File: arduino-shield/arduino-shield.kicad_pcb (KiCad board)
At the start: 2 copper layers, 92 x 61 mm, 15 parts, among them J1 393800102, J2 393800102, J3 393800102, Q1 TIP120, Q2 TIP120, SW1 100SP4T1B2M2QE, SW2 100SP4T1B2M2QE, SW3 ANT13SECQE

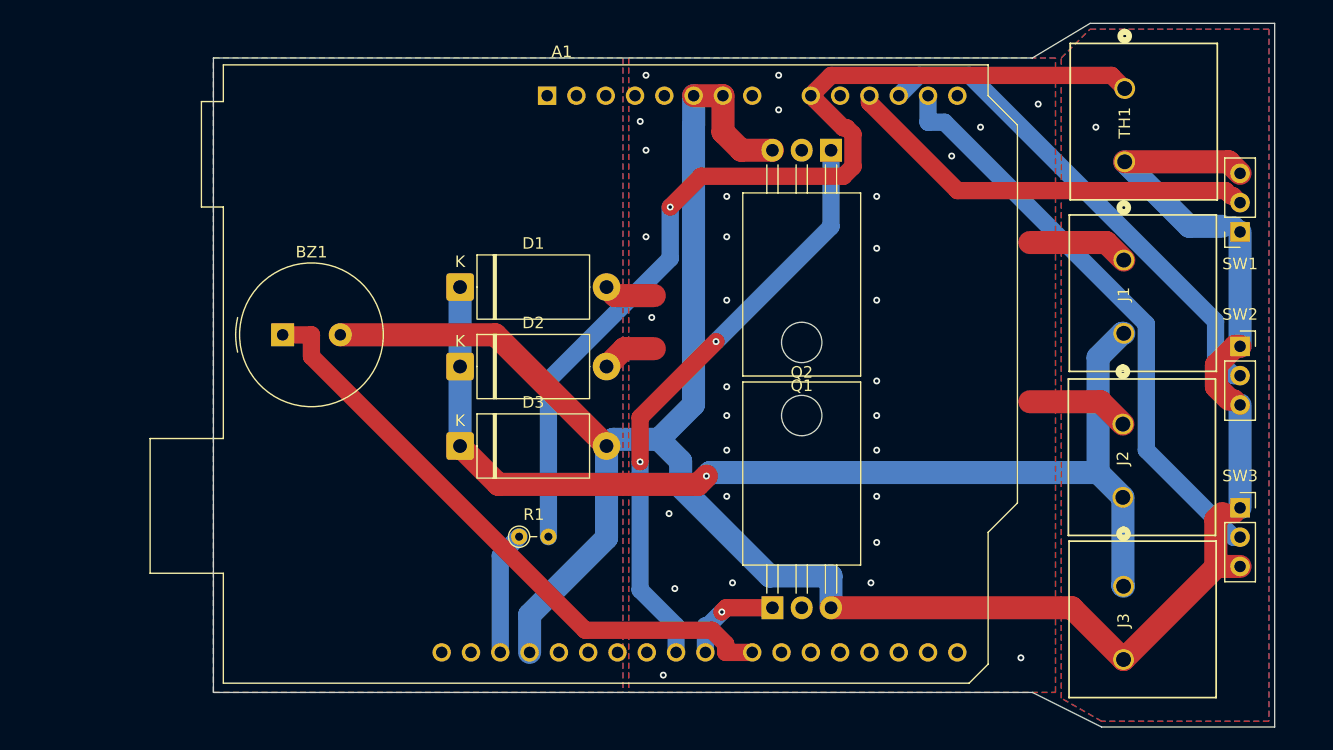
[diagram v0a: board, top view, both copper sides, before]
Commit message: Expand BOM and assembly docs; add shield placement image.
Document DigiKey line items, step-by-step assembly with arduino-shield.jpg,
nylon M3 mounting for Q1/Q2, and updated shield Gerbers/KiCad exports.

Co-authored-by: Cursor <cursoragent@cursor.com>
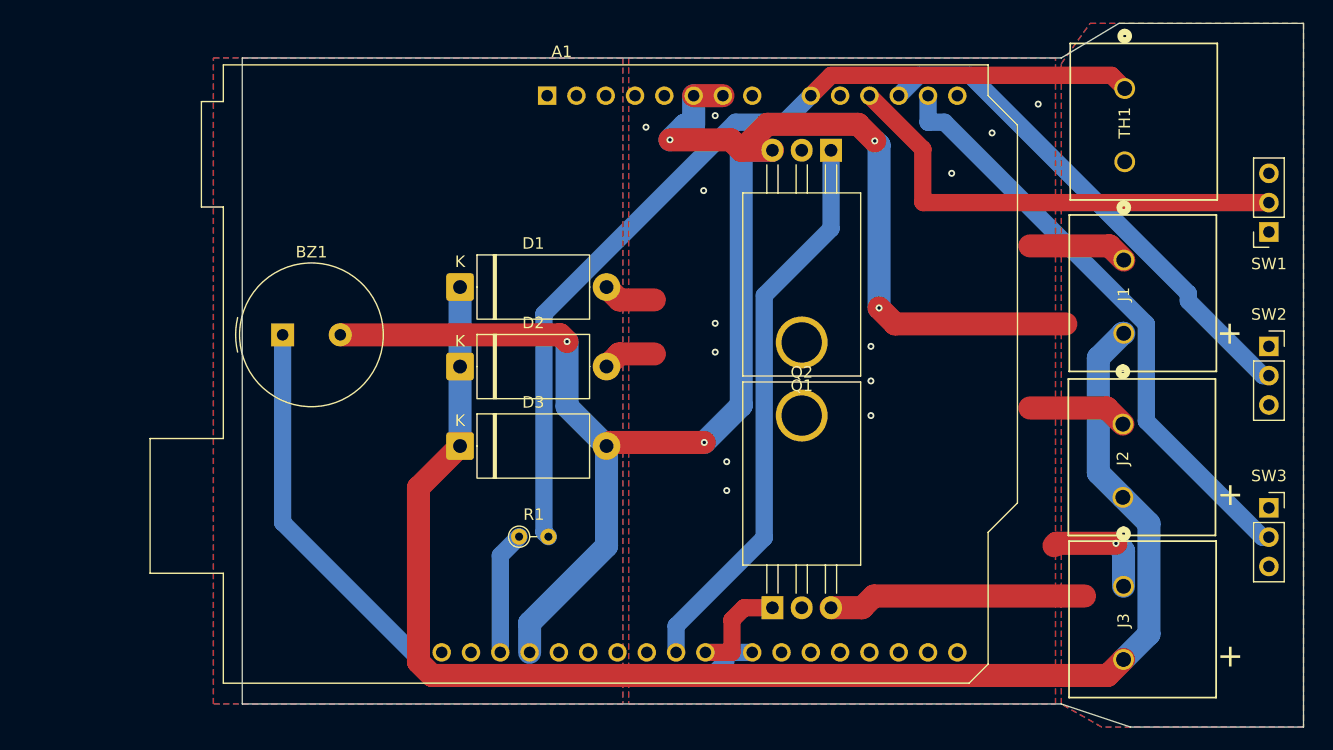
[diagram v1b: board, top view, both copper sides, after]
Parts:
- moved SW1 2.50 mm to (194.5, 82.1)
- moved SW2 2.50 mm to (194.5, 92.0)
- moved SW3 2.50 mm to (194.5, 106.0)
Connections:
- J3 pad 1: 12vdc -> /current
- J3 pad 2: GND -> 12vdc
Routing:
- net GND: track 214.4 -> 172.8 mm, vias 0 -> 5
- net 12vdc: track 94.7 -> 128.1 mm, vias 1 -> 0
- net buzzer+: track 53.6 -> 63.8 mm
- net /current: track 26.9 -> 36.0 mm, vias 31 -> 14
- net Vsense: track 86.5 -> 78.9 mm, vias 1 -> 0
- net temp_up: track 36.3 -> 41.2 mm
- net pump-pwm: track 51.7 -> 49.1 mm, vias 2 -> 0
- net temp_down: track 42.9 -> 44.0 mm
- net relay_control: track 50.6 -> 51.7 mm
- net relay2pin: track 8.76 -> 9.06 mm, vias 1 -> 0
- net (no net): vias 1 -> 0
- added copper zone on B.Cu, net GND
- added copper zone on F.Cu, net GND
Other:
- outline, holes or cut-outs redrawn
- board text added: "+"

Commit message: Update shield layout, placement image, and Gerbers.
Refresh KiCad PCB, silkscreen, and fabrication outputs to match the
current board design shown in arduino-shield.jpg.

Co-authored-by: Cursor <cursoragent@cursor.com>
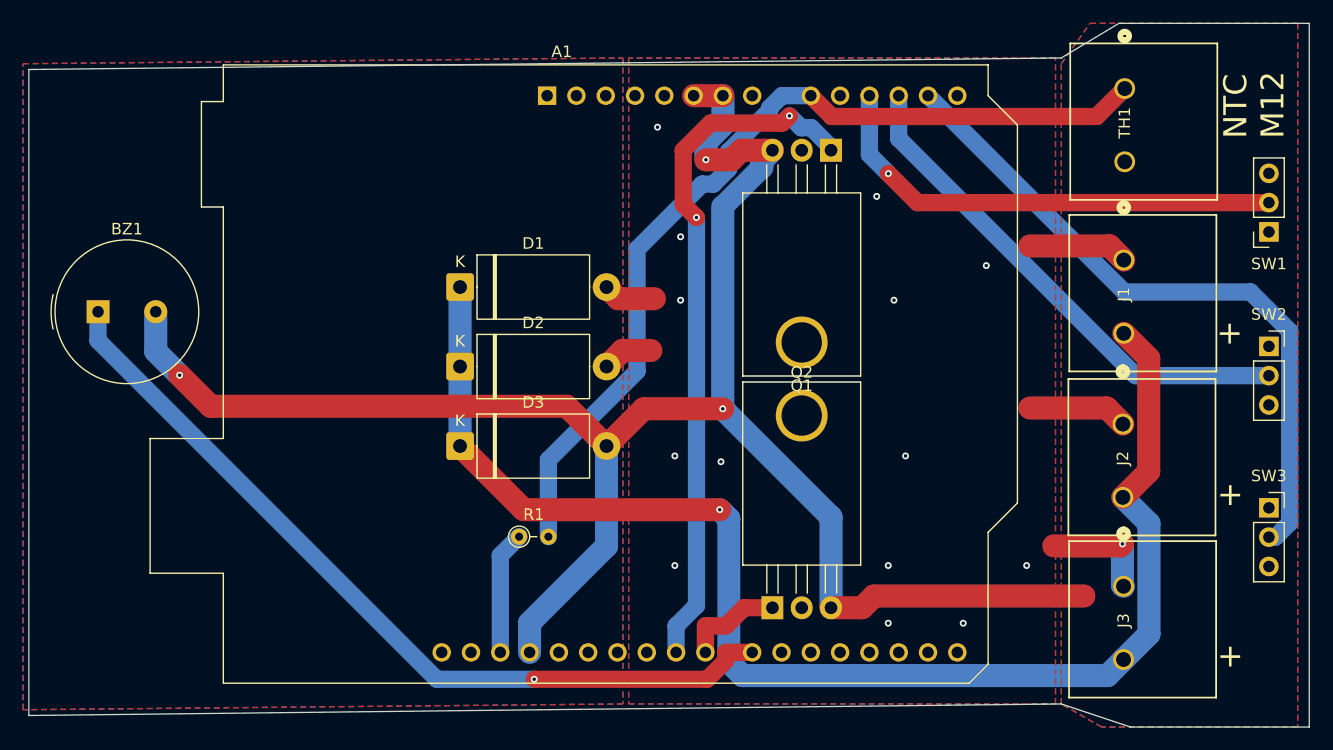
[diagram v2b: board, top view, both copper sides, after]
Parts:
- moved BZ1 16.1 mm to (93.0, 89.0)
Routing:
- net GND: track 172.8 -> 160.5 mm, vias 5 -> 3
- net pump-pwm: track 49.1 -> 60.2 mm, vias 0 -> 2
- net buzzer+: track 63.8 -> 72.8 mm, vias 0 -> 1
- net 12vdc: track 128.1 -> 119.3 mm, vias 0 -> 1
- net relay_control: track 51.7 -> 58.7 mm
- net temp_up: track 41.2 -> 41.5 mm, vias 0 -> 1
- net /current: vias 14 -> 15
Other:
- board size 92 x 61 mm -> 111 x 61 mm
- board text added: "NTC M12"
